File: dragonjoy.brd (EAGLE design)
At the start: 53.3 x 35.2 mm, 12 parts, among them IC1 4066N

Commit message: add 90 degree connector
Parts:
- X1: device con-subd:F09VP -> con-subd:182-009-MALE
- moved X1 7.62 mm to (49.5, 19.1)
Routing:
- net UP: track 33.4 -> 42.5 mm
- net FIRE: track 48.6 -> 57.0 mm
- net FIRE2: track 48.6 -> 57.0 mm
- net DN: track 24.7 -> 30.4 mm
- net RT: track 25.8 -> 31.5 mm
- net N$1: track 29.0 -> 32.0 mm
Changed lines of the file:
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@@
 <element name="R7" library="rcl" package="0207/10" value="" x="12.7" y="15.24" rot="R180"/>
 <element name="R8" library="rcl" package="0207/10" value="" x="12.7" y="27.94" rot="R180"/>
-<element name="X1" library="con-subd" package="F09VP" value="" x="41.91" y="19.05" rot="R90">
-<attribute name="MF" value="" x="41.91" y="19.05" size="1.778" layer="27" rot="R90" display="off"/>
-<attribute name="OC_NEWARK" value="unknown" x="41.91" y="19.05" size="1.778" layer="27" rot="R90" display="off"/>
-<attribute name="MPN" value="" x="41.91" y="19.05" size="1.778" layer="27" rot="R90" display="off"/>
-<attribute name="OC_FARNELL" value="unknown" x="41.91" y="19.05" size="1.778" layer="27" rot="R90" display="off"/>
+<element name="X1" library="con-subd" package="182-009-MALE" value="" x="49.53" y="19.05" rot="R90">
+<attribute name="MF" value="" x="49.53" y="19.05" size="1.778" layer="27" rot="R90" display="off"/>
+<attribute name="OC_NEWARK" value="unknown" x="49.53" y="19.05" size="1.778" layer="27" rot="R90" display="off"/>
+<attribute name="MPN" value="" x="49.53" y="19.05" size="1.778" layer="27" rot="R90" display="off"/>
+<attribute name="OC_FARNELL" value="unknown" x="49.53" y="19.05" size="1.778" layer="27" rot="R90" display="off"/>
 </element>
 <element name="SV1" library="con-lsta" package="FE06" value="" x="2.54" y="19.05" rot="R90">
@@
 <contactref element="R2" pad="1"/>
 <contactref element="X1" pad="4"/>
-<wire x1="40.4876" y1="16.3068" x2="40.4876" y2="16.3576" width="0.508" layer="1"/>
+<wire x1="38.6067" y1="21.8186" x2="40.4876" y2="16.3576" width="0.508" layer="1"/>
 <wire x1="40.4876" y1="16.3576" x2="40.64" y2="16.51" width="0.508" layer="1"/>
 <wire x1="40.64" y1="16.51" x2="39.37" y2="16.51" width="0.508" layer="1"/>
@@
 <contactref element="R3" pad="1"/>
 <contactref element="X1" pad="2"/>
-<wire x1="40.4876" y1="21.7932" x2="40.4876" y2="21.7424" width="0.508" layer="1"/>
+<wire x1="38.6067" y1="16.2814" x2="40.4876" y2="21.7424" width="0.508" layer="1"/>
 <wire x1="40.4876" y1="21.7424" x2="40.64" y2="21.59" width="0.508" layer="1"/>
 <wire x1="40.64" y1="21.59" x2="36.83" y2="21.59" width="0.508" layer="1"/>
@@
 <contactref element="R4" pad="1"/>
 <contactref element="X1" pad="3"/>
-<wire x1="40.4876" y1="19.05" x2="40.64" y2="19.05" width="0.508" layer="16"/>
-<wire x1="40.4876" y1="19.05" x2="35.56" y2="19.05" width="0.508" layer="16"/>
+<wire x1="38.6067" y1="19.05" x2="40.64" y2="19.05" width="0.508" layer="16"/>
+<wire x1="38.6067" y1="19.05" x2="35.56" y2="19.05" width="0.508" layer="16"/>
 <wire x1="35.56" y1="19.05" x2="34.29" y2="17.78" width="0.508" layer="16"/>
 <wire x1="34.29" y1="17.78" x2="29.21" y2="17.78" width="0.508" layer="16"/>
@@
 <contactref element="R5" pad="1"/>
 <contactref element="X1" pad="1"/>
-<wire x1="40.4876" y1="24.5364" x2="38.5064" y2="24.5364" width="0.508" layer="16"/>
+<wire x1="38.6067" y1="13.5128" x2="38.5064" y2="24.5364" width="0.508" layer="16"/>
 <wire x1="34.29" y1="20.32" x2="29.21" y2="20.32" width="0.508" layer="16"/>
 <wire x1="29.21" y1="20.32" x2="25.4" y2="16.51" width="0.508" layer="16"/>
@@
 <wire x1="38.1" y1="30.48" x2="43.18" y2="25.4" width="0.508" layer="1"/>
 <wire x1="43.18" y1="25.4" x2="43.18" y2="23.3172" width="0.508" layer="1"/>
-<wire x1="43.18" y1="23.3172" x2="43.3324" y2="23.1648" width="0.508" layer="1"/>
+<wire x1="43.18" y1="23.3172" x2="41.4503" y2="14.8971" width="0.508" layer="1"/>
 </signal>
 <signal name="FIRE2">
@@
 <wire x1="38.1" y1="7.62" x2="43.18" y2="12.7" width="0.508" layer="1"/>
 <wire x1="43.18" y1="12.7" x2="43.18" y2="14.7828" width="0.508" layer="1"/>
-<wire x1="43.18" y1="14.7828" x2="43.3324" y2="14.9352" width="0.508" layer="1"/>
+<wire x1="43.18" y1="14.7828" x2="41.4503" y2="23.2029" width="0.508" layer="1"/>
 </signal>
 <signal name="N$1">
 <contactref element="JP1" pad="1"/>
 <contactref element="X1" pad="7"/>
-<wire x1="43.3324" y1="20.4216" x2="44.3484" y2="20.4216" width="0.508" layer="16"/>
+<wire x1="41.4503" y1="17.6657" x2="44.3484" y2="20.4216" width="0.508" layer="16"/>
 <wire x1="44.3484" y1="20.4216" x2="45.72" y2="19.05" width="0.508" layer="16"/>
 <wire x1="45.72" y1="19.05" x2="45.72" y2="12.7" width="0.508" layer="16"/>

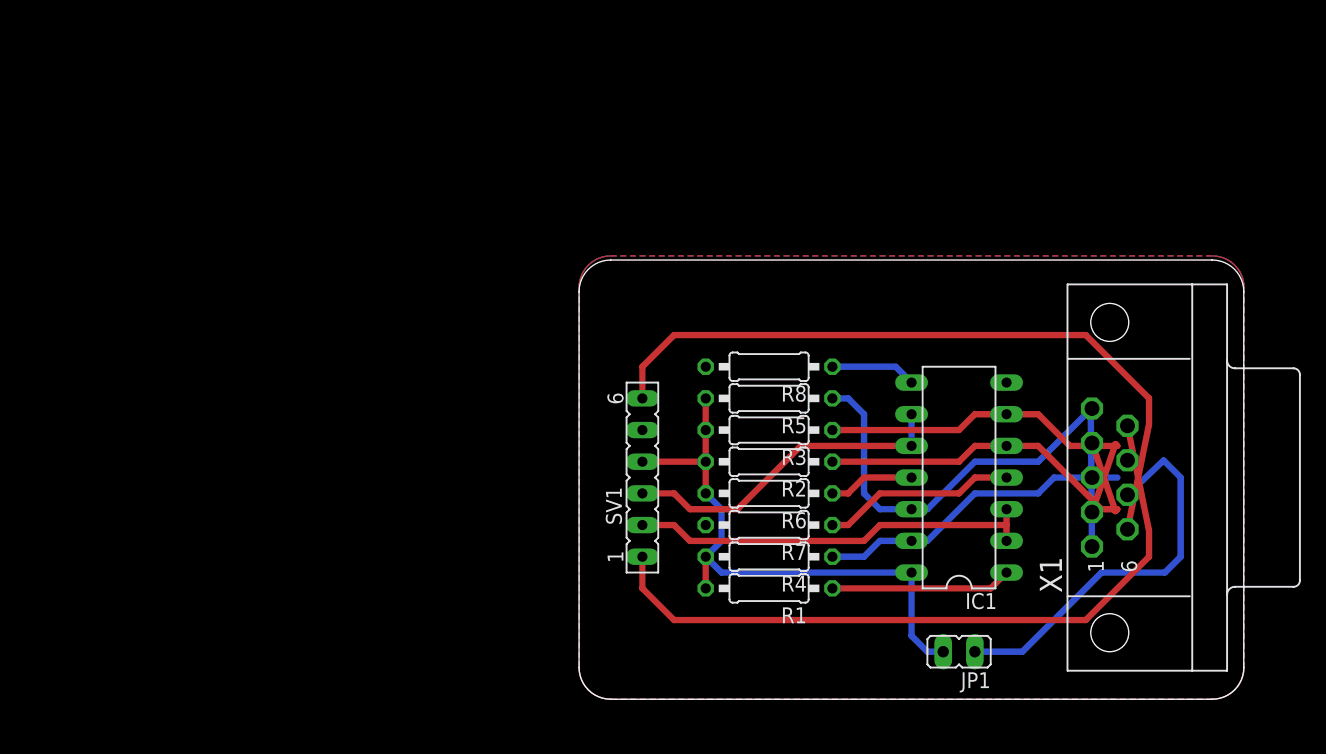
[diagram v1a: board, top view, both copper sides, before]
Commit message: double up board elements at schematic level
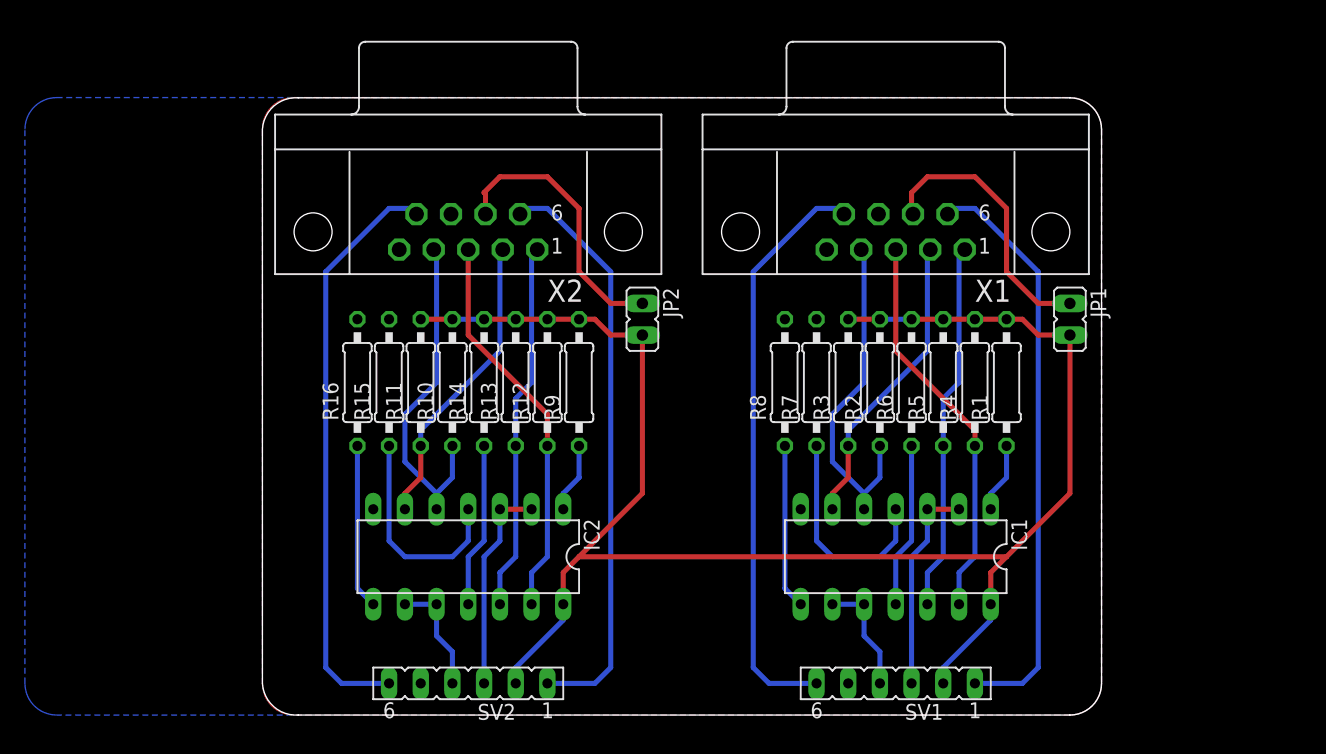
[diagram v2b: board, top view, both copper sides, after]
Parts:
- added IC2: 4066N, 40xx:DIL14
- added JP2: (no value), jumper:JP1
- added R10, R11, R12, R13, R14, R15, R16, R9: (no value), rcl:0207/10
- added SV2: (no value), con-lsta:FE06
- added X2: (no value), con-subd:182-009-MALE
- moved X1 39.6 mm to (22.9, 48.3), turned to 180 degrees
- moved JP1 28.1 mm to (36.8, 31.8), turned to 180 degrees
- moved SV1 26.2 mm to (22.9, 2.54), turned to 180 degrees
- moved R1 25.2 mm to (31.8, 26.7), turned to 90 degrees
- moved R4 21.6 mm to (29.2, 26.7), turned to 90 degrees
- moved R6 14.5 mm to (24.1, 26.7), turned to 90 degrees
- moved R5 14.0 mm to (26.7, 26.7), turned to 90 degrees
- moved R7 12.0 mm to (16.5, 26.7), turned to 90 degrees
- moved R2 10.9 mm to (21.6, 26.7), turned to 90 degrees
- moved IC1 8.13 mm to (22.9, 12.7), turned to 180 degrees
- moved R3 7.41 mm to (19.1, 26.7), turned to 90 degrees
- moved R8 1.80 mm to (14.0, 26.7), turned to 90 degrees
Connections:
- new net DN-R: IC2.6, R11.1, X2.2
- new net FIRE-R: SV2.1, X2.6
- new net FIRE2-R: SV2.6, X2.9
- new net LT-R: IC2.13, R12.1, X2.3
- new net N$2: IC2.1, R9.1
- new net N$4: IC2.11, R14.1
- new net N$5: IC2.4, R15.1
- new net N$6: IC2.8, R16.1
- new net N$7: JP2.1, X2.7
- new net RT-R: IC2.5, R10.1, X2.4
- new net UP-R: IC2.12, R13.1, X2.1
- new net X-R: IC2.2, IC2.3, SV2.3
- new net Y-R: IC2.10, IC2.9, SV2.4
- net FIRE: now also SV1.1; no longer SV1.6
- net FIRE2: now also SV1.6; no longer SV1.1
- net GND: now also IC2.7, R15.2, R16.2, SV2.5, X2.8
- net VCC: now also IC2.14, JP2.2, R10.2, R11.2, R12.2, R13.2, R14.2, R9.2, SV1.2, SV2.2; no longer SV1.4
- net X: now also SV1.3; no longer SV1.2
- net Y: now also SV1.4; no longer SV1.3
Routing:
- net VCC: track 46.6 -> 135.2 mm
- net FIRE2-R: track 0.00 -> 46.9 mm
- net FIRE-R: track 0.00 -> 46.9 mm
- net LT-R: track 0.00 -> 31.6 mm
- net UP-R: track 0.00 -> 29.7 mm
- net RT-R: track 0.00 -> 27.4 mm
- net DN-R: track 0.00 -> 24.1 mm
- net N$7: track 0.00 -> 22.2 mm
- net N$5: track 0.00 -> 17.6 mm
- net Y: track 26.8 -> 9.42 mm
- net X-R: track 0.00 -> 17.0 mm
- net X: track 32.8 -> 17.0 mm
- net N$6: track 0.00 -> 13.2 mm
- net N$4: track 0.00 -> 13.2 mm
- net UP: track 42.5 -> 29.7 mm
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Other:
- board size 53.3 x 35.2 mm -> 67.3 x 49.5 mm

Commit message: prepare for submission
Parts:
- moved JP1 7.73 mm to (29.2, 33.0)
- moved R1 6.48 mm to (25.4, 27.9)
- moved R3 6.48 mm to (12.7, 27.9)
- moved R4 6.48 mm to (22.9, 27.9)
- moved R5 6.48 mm to (20.3, 27.9)
- moved R7 6.48 mm to (10.2, 27.9)
- moved R8 6.48 mm to (7.62, 27.9)
- moved JP2 6.48 mm to (-3.81, 33.0)
- moved R2 6.48 mm to (15.2, 27.9)
- moved IC1 6.48 mm to (16.5, 14.0)
- moved R6 6.48 mm to (17.8, 27.9)
- moved SV1 6.48 mm to (16.5, 3.81)
- moved X1 6.48 mm to (16.5, 49.5)
- moved IC2 5.24 mm to (-16.5, 14.0)
- moved R10 5.24 mm to (-17.8, 27.9)
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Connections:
- net N$7 renamed N$7-R
- new net VCC-R: IC2.14, JP2.2, R10.2, R11.2, R12.2, R13.2, R14.2, R9.2, SV2.2
- net VCC: no longer IC2.14, JP2.2, R10.2, R11.2, R12.2, R13.2, R14.2, R9.2, SV2.2
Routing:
- net VCC: track 135.2 -> 48.4 mm
- net VCC-R: track 0.00 -> 48.4 mm
- net FIRE-R: track 46.9 -> 45.1 mm
- net FIRE: track 46.9 -> 45.1 mm
- net N$7-R: track 22.2 -> 20.9 mm
- net N$1: track 22.2 -> 20.9 mm
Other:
- board size 67.3 x 49.5 mm -> 66 x 50.8 mm
- board text added: "4066"
- board text added: "Digital Joystick Adapter"
- board text added: "Dragon / Coco"
